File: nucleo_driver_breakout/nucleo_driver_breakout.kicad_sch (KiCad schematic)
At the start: 95 parts, among them J1 Conn_02x18_Odd_Even, J10 Conn_01x06_Pin, J11 Conn_01x06_Pin, J12 Conn_01x04_Pin, J13 Conn_01x04_Pin, J14 Conn_01x04_Pin, J15 Conn_01x04_Pin, J2 Conn_02x18_Odd_Even, J3 ENC_1, J4 ENC_2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

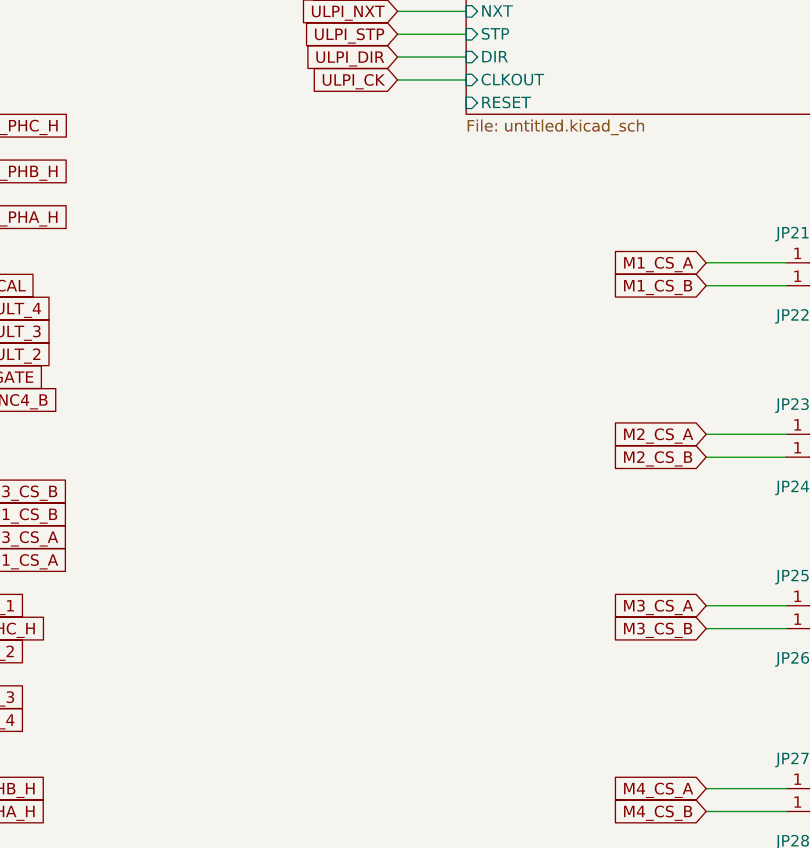
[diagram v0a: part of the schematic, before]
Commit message: added current sense header for each motor
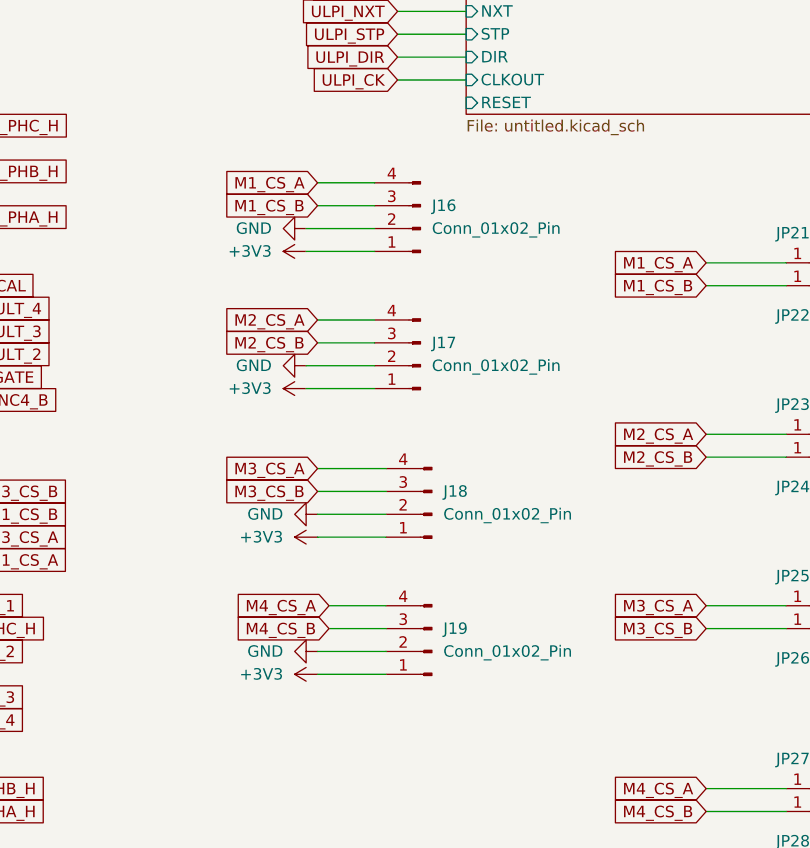
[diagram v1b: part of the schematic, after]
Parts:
- added J16, J17, J18, J19: Conn_01x02_Pin, Connector_JST:JST_EH_B4B-EH-A_1x04_P2.50mm_Vertical, symbol Connector:Conn_01x04_Pin
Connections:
- net +3V3: now also J16.1 (Pin_1), J17.1 (Pin_1), J18.1 (Pin_1), J19.1 (Pin_1)
- net GND: now also J16.2 (Pin_2), J17.2 (Pin_2), J18.2 (Pin_2), J19.2 (Pin_2)
- net M1_CS_A: now also J16.4 (Pin_4)
- net M1_CS_B: now also J16.3 (Pin_3)
- net M2_CS_A: now also J17.4 (Pin_4)
- net M2_CS_B: now also J17.3 (Pin_3)
- net M3_CS_A: now also J18.4 (Pin_4)
- net M3_CS_B: now also J18.3 (Pin_3)
- net M4_CS_A: now also J19.4 (Pin_4)
- net M4_CS_B: now also J19.3 (Pin_3)

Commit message: changed usb connector and added LCSC IDs
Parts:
- C1, C13, C14, C15, C16, C17, C18, C2, C3, C4, C5, C6: LCSC ID (none) -> C1525
- R1, R10, R11, R12, R13, R14, R15, R2, R21, R22, R23, R24, R25, R26, R30, R31, R32, R33, R34, R35, R4, R5, R6, R7: LCSC ID (none) -> C11702
- R16, R17, R18, R27, R28, R29, R3, R36, R37, R38, R8, R9: LCSC ID (none) -> C25079
- U1: now left out of the parts list
- U2, U3, U5, U6: LCSC ID (none) -> C524786

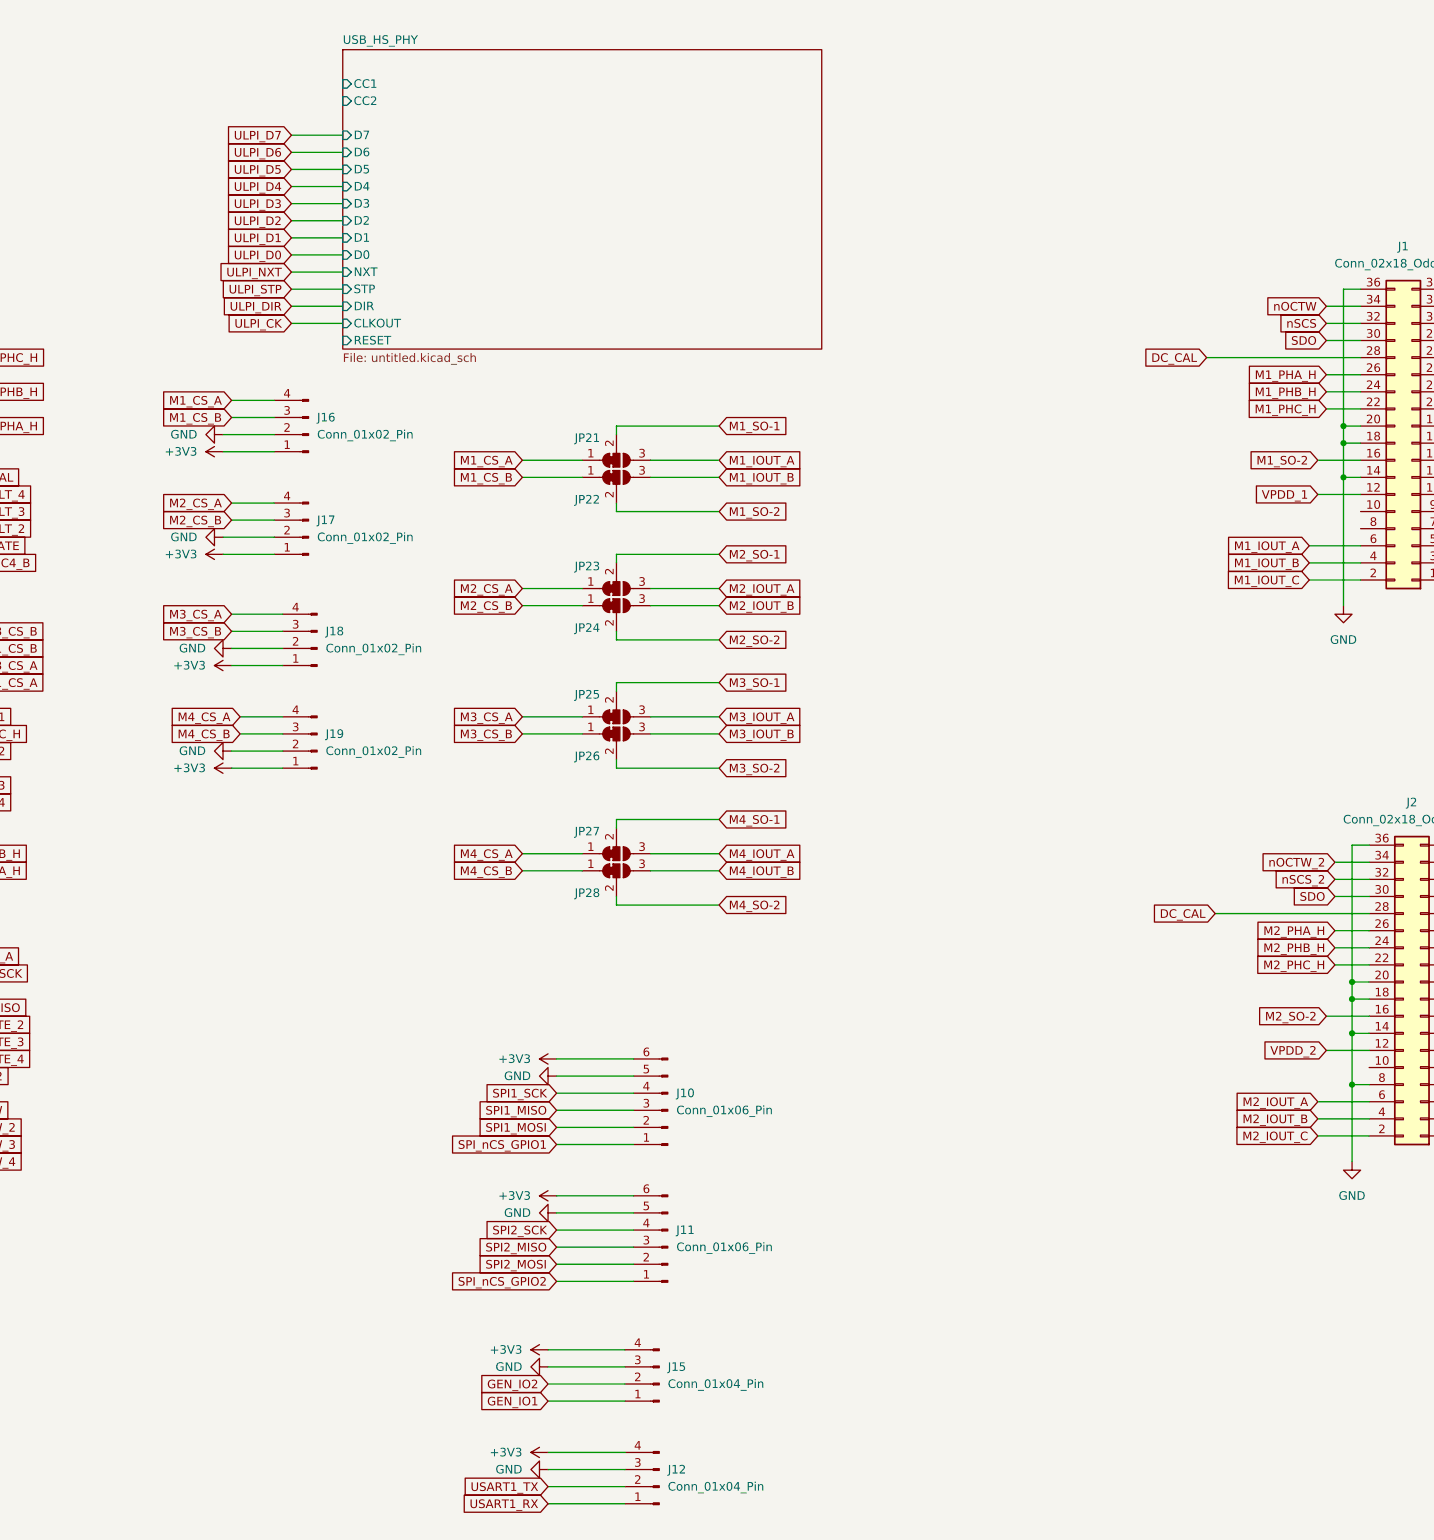
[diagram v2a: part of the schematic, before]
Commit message: added bolt holes, vias, and fixed some silkscreen overlaps
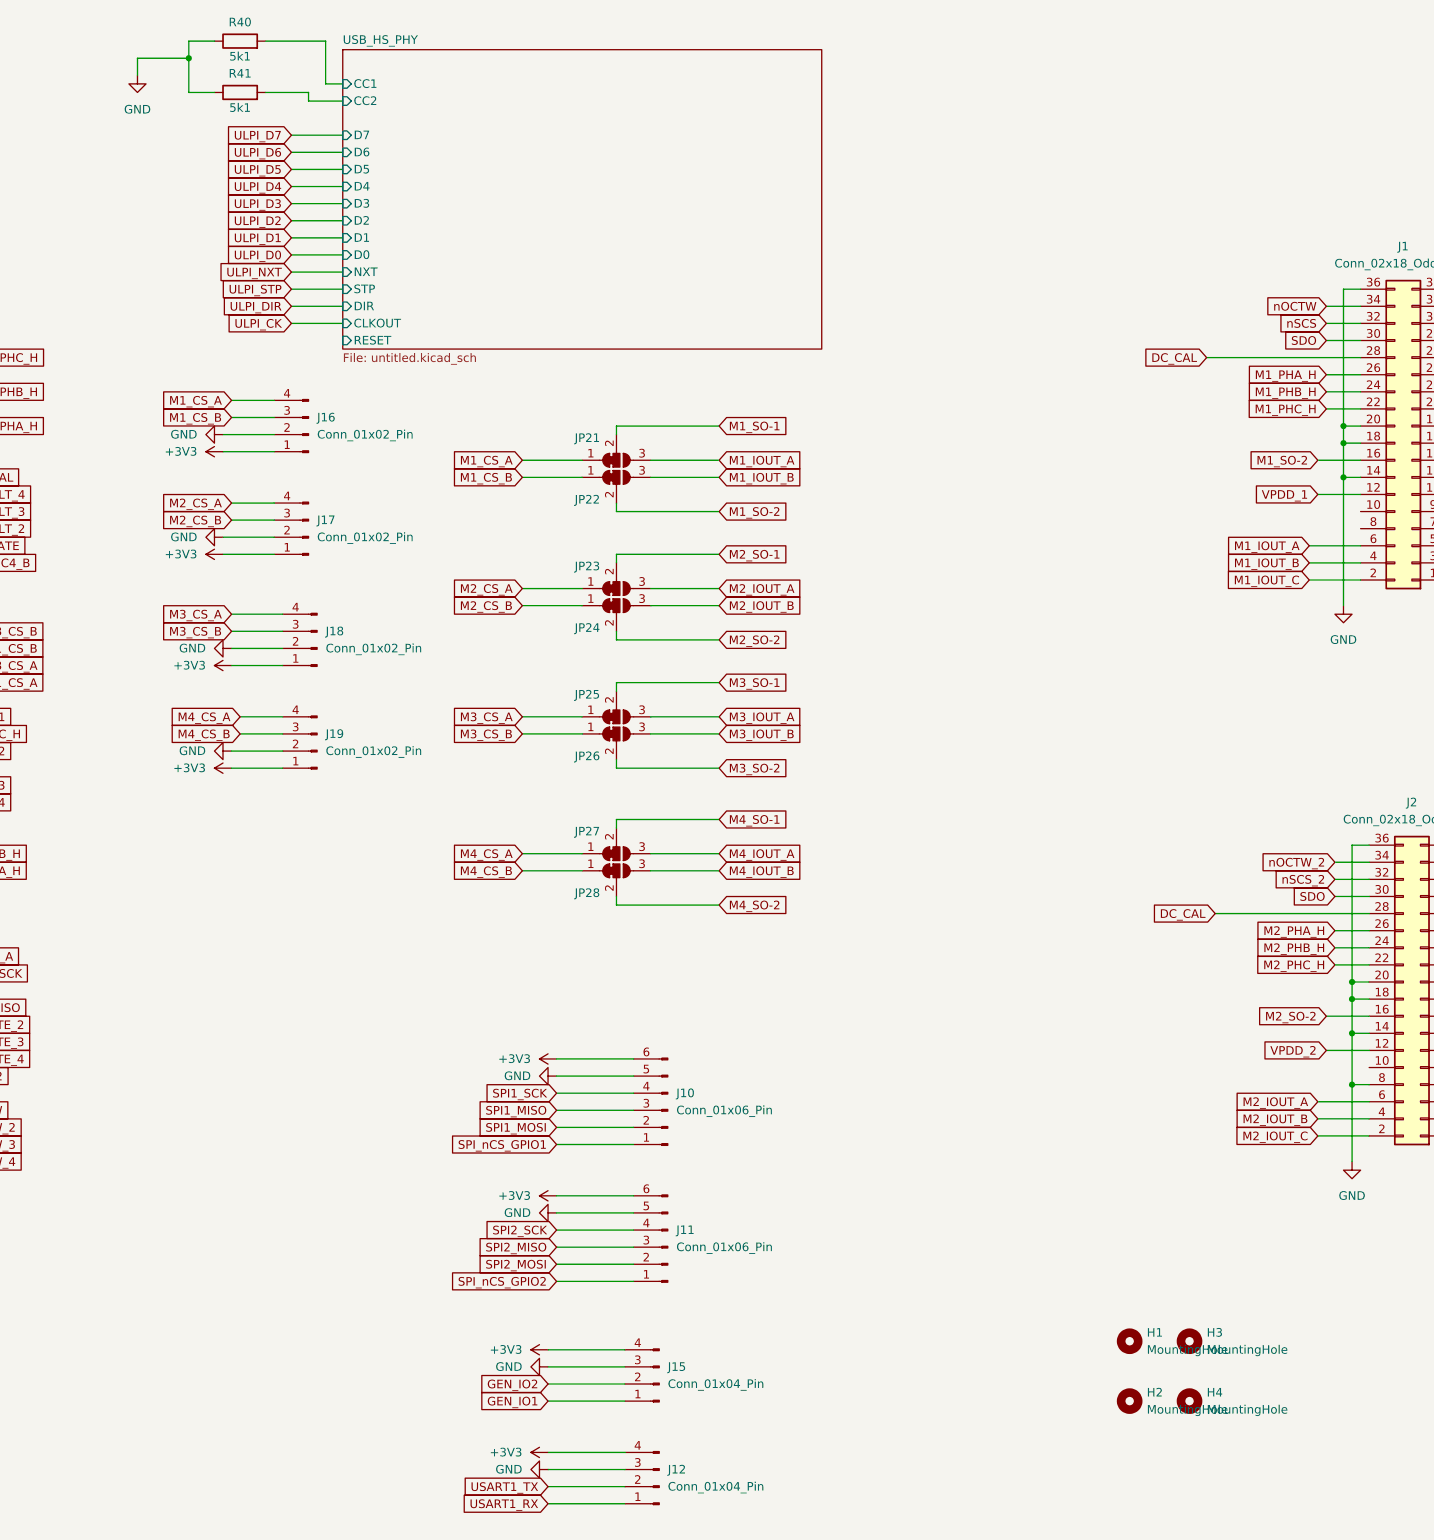
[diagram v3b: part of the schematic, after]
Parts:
- added H1, H2, H3, H4: MountingHole, MountingHole:MountingHole_3.2mm_M3_ISO7380, symbol Mechanical:MountingHole
- added R40, R41: 5k1, Resistor_SMD:R_0402_1005Metric, symbol Device:R
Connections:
- net GND: now also R40.1, R41.1
- net USB_HS_PHY/CC1: now also R40.2
- net USB_HS_PHY/CC2: now also R41.2

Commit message: changed termination resistors to 1206 and added gitignore
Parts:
- R16, R17, R18, R27, R28, R29, R3, R36, R37, R38, R8, R9: footprint Resistor_SMD:R_0402_1005Metric -> Resistor_SMD:R_1206_3216Metric; LCSC ID C25079 -> C17909
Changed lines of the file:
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@@
 			)
 		)
-		(property "Footprint" "Resistor_SMD:R_0402_1005Metric"
+		(property "Footprint" "Resistor_SMD:R_1206_3216Metric"
 			(at 361.95 380.238 90)
 			(effects
@@
 			)
 		)
-		(property "LCSC ID" "C25079"
+		(property "LCSC ID" "C17909"
 			(at 361.95 378.46 0)
 			(effects
@@
 			)
 		)
-		(property "Footprint" "Resistor_SMD:R_0402_1005Metric"
+		(property "Footprint" "Resistor_SMD:R_1206_3216Metric"
 			(at 483.87 295.148 90)
 			(effects
@@
 			)
 		)
-		(property "LCSC ID" "C25079"
+		(property "LCSC ID" "C17909"
 			(at 483.87 293.37 0)
 			(effects
@@
 			)
 		)
-		(property "Footprint" "Resistor_SMD:R_0402_1005Metric"
+		(property "Footprint" "Resistor_SMD:R_1206_3216Metric"
 			(at 102.87 366.268 90)
 			(effects
@@
 			)
 		)
-		(property "LCSC ID" "C25079"
+		(property "LCSC ID" "C17909"
 			(at 102.87 364.49 0)
 			(effects
@@
 			)
 		)
-		(property "Footprint" "Resistor_SMD:R_0402_1005Metric"
+		(property "Footprint" "Resistor_SMD:R_1206_3216Metric"
 			(at 361.95 352.298 90)
 			(effects
@@
 			)
 		)
-		(property "LCSC ID" "C25079"
+		(property "LCSC ID" "C17909"
 			(at 361.95 350.52 0)
 			(effects
@@
 			)
 		)
-		(property "Footprint" "Resistor_SMD:R_0402_1005Metric"
+		(property "Footprint" "Resistor_SMD:R_1206_3216Metric"
 			(at 231.14 359.918 90)
 			(effects
@@
 			)
 		)
-		(property "LCSC ID" "C25079"
+		(property "LCSC ID" "C17909"
 			(at 231.14 358.14 0)
 			(effects
@@
 			)
 		)
-		(property "Footprint" "Resistor_SMD:R_0402_1005Metric"
+		(property "Footprint" "Resistor_SMD:R_1206_3216Metric"
 			(at 102.87 358.648 90)
 			(effects
@@
 			)
 		)
-		(property "LCSC ID" "C25079"
+		(property "LCSC ID" "C17909"
 			(at 102.87 356.87 0)
 			(effects
@@
 			)
 		)
-		(property "Footprint" "Resistor_SMD:R_0402_1005Metric"
+		(property "Footprint" "Resistor_SMD:R_1206_3216Metric"
 			(at 102.87 386.588 90)
 			(effects
@@
 			)
 		)
-		(property "LCSC ID" "C25079"
+		(property "LCSC ID" "C17909"
 			(at 102.87 384.81 0)
 			(effects
@@
 			)
 		)
-		(property "Footprint" "Resistor_SMD:R_0402_1005Metric"
+		(property "Footprint" "Resistor_SMD:R_1206_3216Metric"
 			(at 483.87 302.768 90)
 			(effects
@@
 			)
 		)
-		(property "LCSC ID" "C25079"
+		(property "LCSC ID" "C17909"
 			(at 483.87 300.99 0)
 			(effects
@@
 			)
 		)
-		(property "Footprint" "Resistor_SMD:R_0402_1005Metric"
+		(property "Footprint" "Resistor_SMD:R_1206_3216Metric"
 			(at 231.14 367.538 90)
 			(effects
@@
 			)
 		)
-		(property "LCSC ID" "C25079"
+		(property "LCSC ID" "C17909"
 			(at 231.14 365.76 0)
 			(effects
@@
 			)
 		)
-		(property "Footprint" "Resistor_SMD:R_0402_1005Metric"
+		(property "Footprint" "Resistor_SMD:R_1206_3216Metric"
 			(at 361.95 359.918 90)
 			(effects
@@
 			)
 		)
-		(property "LCSC ID" "C25079"
+		(property "LCSC ID" "C17909"
 			(at 361.95 358.14 0)
 			(effects
@@
 			)
 		)
-		(property "Footprint" "Resistor_SMD:R_0402_1005Metric"
+		(property "Footprint" "Resistor_SMD:R_1206_3216Metric"
 			(at 483.87 323.088 90)
 			(effects
@@
 			)
 		)
-		(property "LCSC ID" "C25079"
+		(property "LCSC ID" "C17909"
 			(at 483.87 321.31 0)
 			(effects
@@
 			)
 		)
-		(property "Footprint" "Resistor_SMD:R_0402_1005Metric"
+		(property "Footprint" "Resistor_SMD:R_1206_3216Metric"
 			(at 231.14 387.858 90)
 			(effects
@@
 			)
 		)
-		(property "LCSC ID" "C25079"
+		(property "LCSC ID" "C17909"
 			(at 231.14 386.08 0)
 			(effects
